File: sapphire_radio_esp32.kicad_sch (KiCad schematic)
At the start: 105 parts, among them IC1 AZ1117CH-3.3TRG1, J1 USB4105-GF-A, J2 Screw_Terminal_01x02, J3 FAKRA, J4 Screw_Terminal_01x02, J5 Screw_Terminal_01x02, Q1 DMG2305UX-7, Q3 2N7002PS_115, U1 ESP32-WROOM-32E-N8R2, U2 CP2102N-A02-GQFN24R, U4 SI4735, U5 NC7WZ14P6X, U6 TMUX1574PWR, U7 PCM5122PWR, U8 MAX9744ETH_

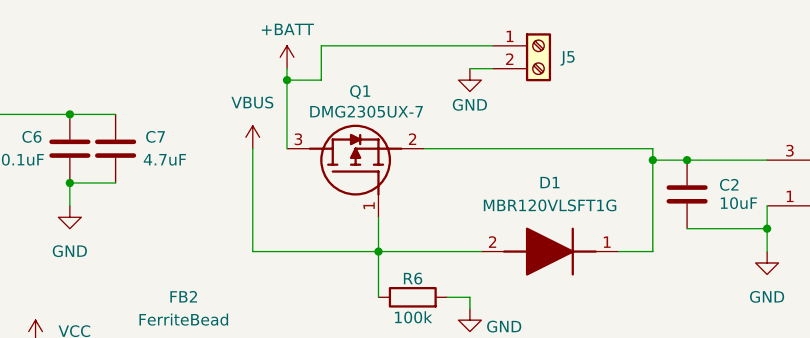
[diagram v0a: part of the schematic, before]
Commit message: Add fuse holder
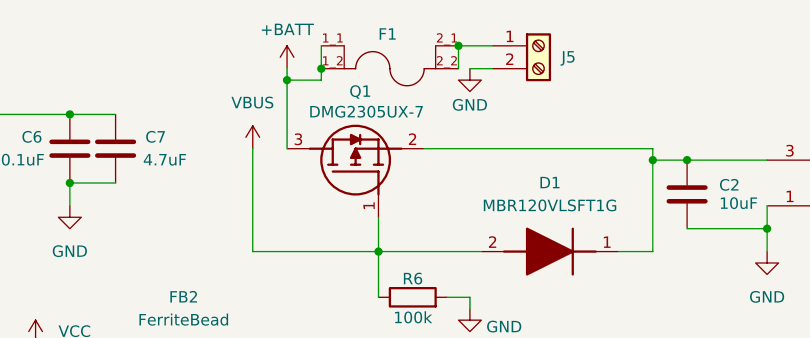
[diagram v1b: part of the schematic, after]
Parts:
- added F1: 3549-2, carter_kicad_footprints:FUSE_3549-2, symbol carter_kicad_symbols:3549-2 Mini Fuse Holder
- C10, C39: DigikeyPN (none) -> 732-8511-1-ND; MFN (none) -> Würth Elektronik; MPN (none) -> 865080545012
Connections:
- net +BATT: now also F1.1_1, F1.1_2; no longer J5.1 (Pin_1)
- new net: F1.2_1, F1.2_2, J5.1 (Pin_1)
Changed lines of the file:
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@@
 	(title_block
 		(title "Volkswagen Sapphire Radio Conversion")
-		(date "2026-03-21")
+		(date "2026-03-27")
 		(rev "1")
 		(company "Carter Harris - KE8OHO")
@@
 	)
 	(junction
+		(at 184.15 17.78)
+		(diameter 0)
+		(color 0 0 0 0)
+	)
+	(junction
 		(at 294.64 154.94)
 		(diameter 0)
@@
 	)
 	(junction
+		(at 199.39 15.24)
+		(diameter 0)
+		(color 0 0 0 0)
+	)
+	(junction
 		(at 153.67 113.03)
 		(diameter 0)
@@
 	(wire
 		(pts
+			(xy 184.15 15.24) (xy 184.15 17.78)
+		)
+		(stroke
+			(width 0)
+			(type default)
+		)
+	)
+	(wire
+		(pts
 			(xy 100.33 168.91) (xy 107.95 168.91)
 		)
@@
 	(wire
 		(pts
+			(xy 199.39 15.24) (xy 199.39 17.78)
+		)
+		(stroke
+			(width 0)
+			(type default)
+		)
+	)
+	(wire
+		(pts
 			(xy 226.06 142.24) (xy 232.41 142.24)
 		)
@@
 	(wire
 		(pts
+			(xy 199.39 15.24) (xy 203.2 15.24)
+		)
+		(stroke
+			(width 0)
+			(type default)
+		)
+	)
+	(wire
+		(pts
 			(xy 302.26 57.15) (xy 302.26 54.61)
 		)
@@
 	(wire
 		(pts
-			(xy 203.2 15.24) (xy 184.15 15.24)
-		)
-		(stroke
-			(width 0)
-			(type default)
-		)
-	)
-	(wire
-		(pts
 			(xy 294.64 71.12) (xy 294.64 67.31)
 		)
@@
 	(wire
 		(pts
-			(xy 184.15 15.24) (xy 184.15 19.05)
-		)
-		(stroke
-			(width 0)
-			(type default)
-		)
-	)
-	(wire
-		(pts
 			(xy 153.67 100.33) (xy 153.67 102.87)
 		)
@@
 	(wire
 		(pts
+			(xy 184.15 17.78) (xy 184.15 19.05)
+		)
+		(stroke
+			(width 0)
+			(type default)
+		)
+	)
+	(wire
+		(pts
 			(xy 334.01 97.79) (xy 337.82 97.79)
 		)
@@
 	)
 	(symbol
+		(lib_id "carter_kicad_symbols:3549-2 Mini Fuse Holder")
+		(at 191.77 17.78 0)
+		(unit 1)
+		(exclude_from_sim no)
+		(in_bom yes)
+		(on_board yes)
+		(dnp no)
+		(property "Reference" "F1"
+			(at 191.516 13.97 0)
+			(effects
+				(font
+					(size 1.27 1.27)
+				)
+			)
+		)
+		(property "Value" "3549-2"
+			(at 189.23 22.86 0)
+			(effects
+				(font
+					(size 1.27 1.27)
+				)
+				(justify left bottom)
+				(hide yes)
+			)
+		)
+		(property "Footprint" "carter_kicad_footprints:FUSE_3549-2"
+			(at 192.024 5.842 0)
+			(effects
+				(font
+					(size 1.27 1.27)
+				)
+				(justify bottom)
+				(hide yes)
+			)
+		)
+		(property "Datasheet" "https://www.keyelco.com/userAssets/file/K75p48.pdf"
+			(at 191.77 17.78 0)
+			(effects
+				(font
+					(size 1.27 1.27)
+				)
+				(hide yes)
+			)
+		)
+		(property "Description" "Fuse Block 20 A 500V 1 Circuit Blade Through Hole"
+			(at 191.77 17.78 0)
+			(effects
+				(font
+					(size 1.27 1.27)
+				)
+				(hide yes)
+			)
+		)
+		(property "MFN" "Keystone Electronics"
+			(at 192.024 5.842 0)
+			(effects
+				(font
+					(size 1.27 1.27)
+				)
+				(justify bottom)
+				(hide yes)
+			)
+		)
+		(property "MPN" "3549-2"
+			(at 191.77 17.78 0)
+			(effects
+				(font
+					(size 1.27 1.27)
+				)
+				(hide yes)
+			)
+		)
+		(property "DigikeyPN" "36-3549-2-ND"
+			(at 191.77 17.78 0)
+			(effects
+				(font
+					(size 1.27 1.27)
+				)
+				(hide yes)
+			)
+		)
+		(property "LCSCPN" "C3206081"
+			(at 191.77 17.78 0)
+			(effects
+				(font
+					(size 1.27 1.27)
+				)
+				(hide yes)
+			)
+		)
+		(pin "2_2"
+		)
+		(pin "2_1"
+		)
+		(pin "1_2"
+		)
+		(pin "1_1"
+		)
+		(instances
+			(project ""
+				(path "/b2cc6a8e-d718-44b3-b274-265d252d3f92"
+					(reference "F1")
+					(unit 1)
+				)
+			)
+		)
+	)
+	(symbol
 		(lib_id "Device:C")
 		(at 330.2 115.57 90)
@@
 			)
 		)
+		(property "MFN" "Würth Elektronik"
+			(at 317.5 58.42 0)
+			(effects
+				(font
+					(size 1.27 1.27)
+				)
+				(hide yes)
+			)
+		)
+		(property "MPN" "865080545012"
+			(at 317.5 58.42 0)
+			(effects
+				(font
+					(size 1.27 1.27)
+				)
+				(hide yes)
+			)
+		)
+		(property "DigikeyPN" "732-8511-1-ND"
+			(at 317.5 58.42 0)
+			(effects
+				(font
+					(size 1.27 1.27)
+				)
+				(hide yes)
+			)
+		)
 		(pin "2"
 		)
@@
 			(at 314.96 71.12 0)
 			(effects
+				(font
+					(size 1.27 1.27)
+				)
+				(hide yes)
+			)
+		)
+		(property "MFN" "Würth Elektronik"
+			(at 314.96 71.12 0)
+			(effects
+				(font
+					(size 1.27 1.27)
+				)
+				(hide yes)
+			)
+		)
+		(property "MPN" "865080545012"
+			(at 314.96 71.12 0)
+			(effects
+				(font
+					(size 1.27 1.27)
+				)
+				(hide yes)
+			)
+		)
+		(property "DigikeyPN" "732-8511-1-ND"
+			(at 314.96 71.12 0)
+			(effects

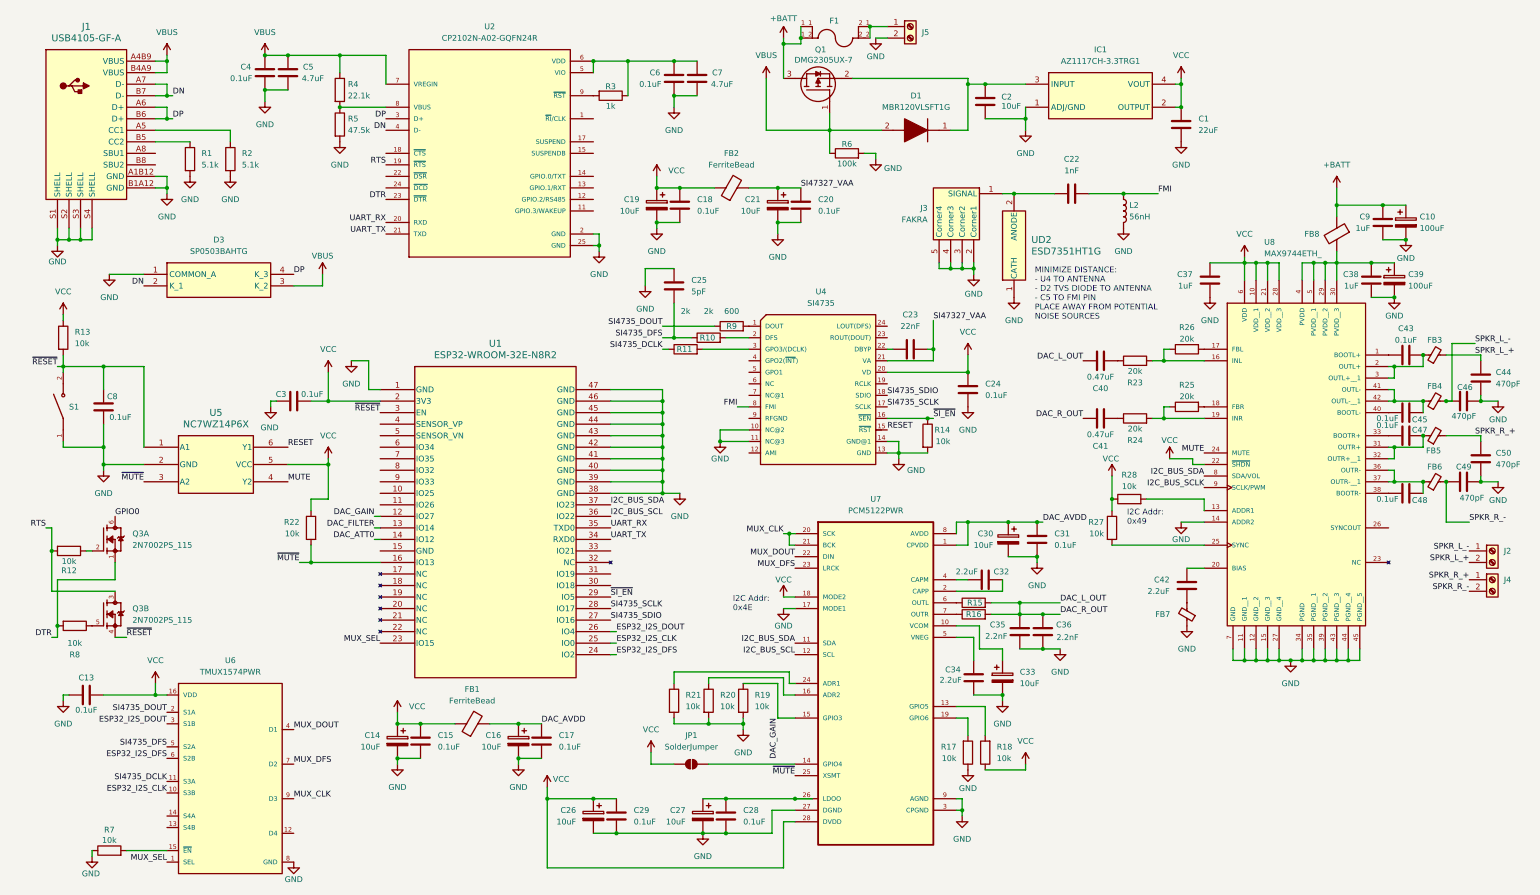
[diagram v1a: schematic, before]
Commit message: Add power filtering and pots
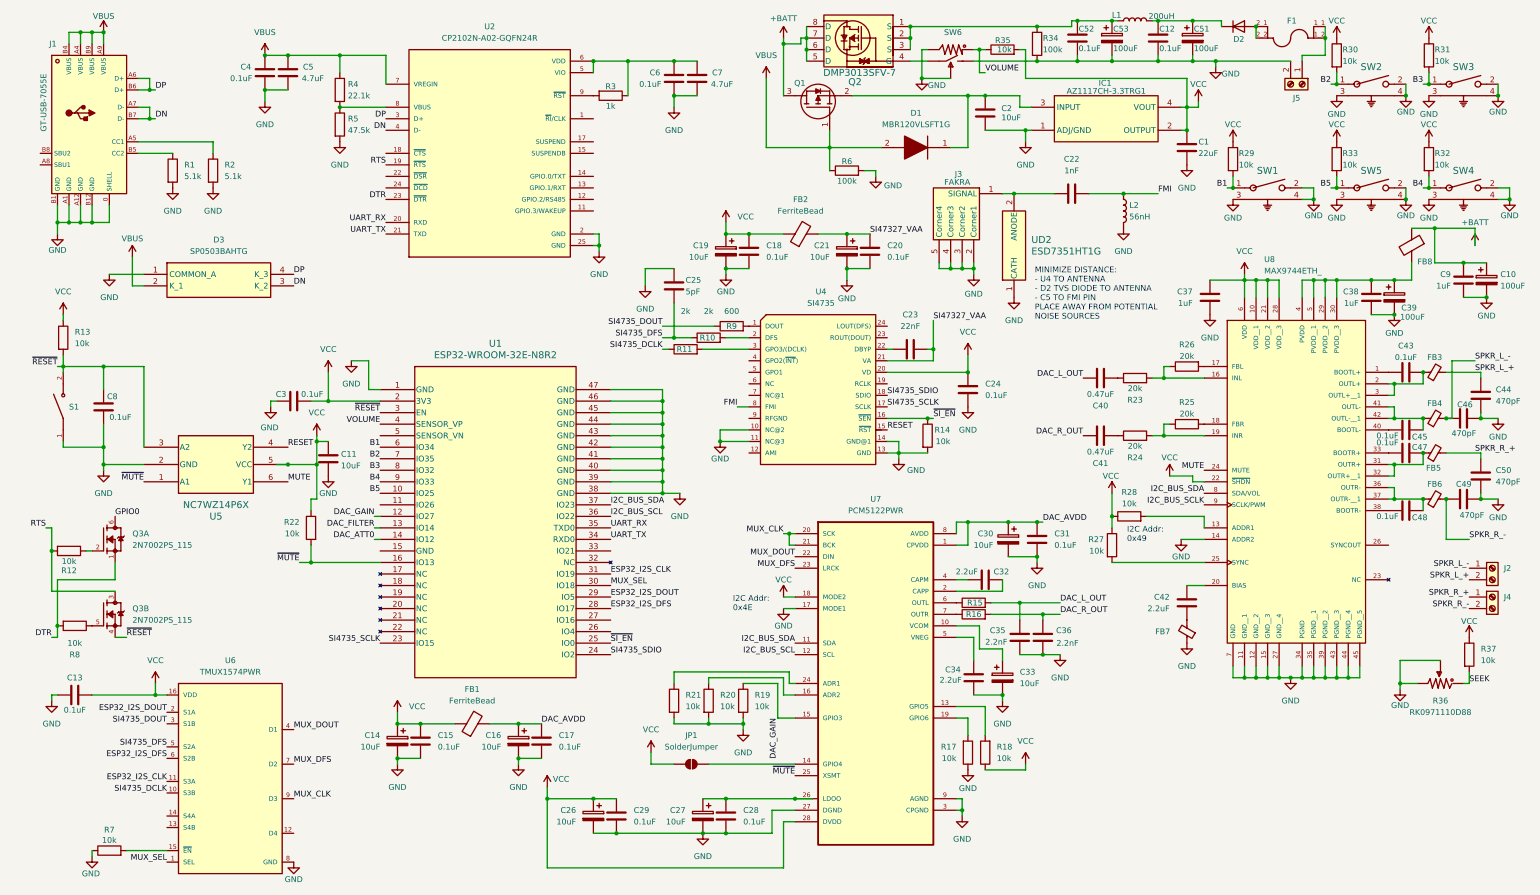
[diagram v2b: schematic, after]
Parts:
- removed J1: USB4105-GF-A, carter_kicad_footprints:USB4105-GF-A_1, symbol carter_kicad_symbols:USB4105-GF-A USB-C Socket
- added C11: 10uF, Capacitor_SMD:C_0603_1608Metric, symbol Device:C
- added C12, C52: 0.1uF, Capacitor_SMD:C_0603_1608Metric, symbol Device:C
- added C51, C53: 100uF, carter_kicad_footprints:CAP_6.3_6.3, symbol Device:C_Polarized
- added D2: D, Package_TO_SOT_SMD:TO-252-2, symbol Device:D
- added J1: GT-USB-7055E, carter_kicad_footprints:USB-C-SMD_GT-USB-7055E, symbol carter_kicad_symbols:GT-USB-7055E USB-C Vertical Socket (LCSC Only)
- added L1: 200uH, carter_kicad_footprints:IND-SMD_L28.0-W25.0-74437529203331, symbol Device:L
- added Q2: DMP3013SFV-7, carter_kicad_footprints:POWERDI3333-8_UX_DIO, symbol carter_kicad_symbols:DMP3013SFV-7 10A P-Channel MOSFET
- added R29, R30, R31, R32, R33, R35, R37: 10k, Resistor_SMD:R_0603_1608Metric, symbol Device:R
- added R34: 100k, Resistor_SMD:R_0603_1608Metric, symbol Device:R
- added R36: RK0971110D88, carter_kicad_footprints:RES-ADJ-TH_RK097111080R, symbol carter_kicad_symbols:RK0971110D88 10k Potentiometer
- added SW1, SW2, SW3, SW4, SW5: 1825027-8, carter_kicad_footprints:SW2_1825027-C_TEC, symbol carter_kicad_symbols:1825027-8 Right Angle Button
- added SW6: RK09711110EL, carter_kicad_footprints:RES-ADJ-TH_RK09711110EL, symbol carter_kicad_symbols:RK09711110EL Potentiometer w/ Rotary Button
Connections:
- net +BATT: now also Q2.5 (D), Q2.6 (D), Q2.7 (D), Q2.8 (D); no longer F1.1_1, F1.1_2
- net DAC_L_OUT: no longer C36.1, C41.1, R16.2
- net DN: now also D3.3 (K_2), J1.A7 (D-), J1.B7 (D-); no longer D3.2 (K_1)
- net DP: now also J1.A6 (D+), J1.B6 (D+)
- net ESP32_I2S_CLK: now also U1.31 (IO19), U6.11 (S3A); no longer U1.25 (IO0), U6.10 (S3B)
- net ESP32_I2S_DFS: now also U1.28 (IO17); no longer U1.24 (IO2)
- net ESP32_I2S_DOUT: now also U1.29 (IO5), U6.2 (S1A); no longer U1.26 (IO4), U6.3 (S1B)
- net GND: now also C11.2, C12.2, C51.2, C52.2, C53.2, J1.0 (SHELL), J1.A1 (GND), J1.A12 (GND), J1.B1 (GND), J1.B12 (GND), R34.2, R36.2, R36.3, SW1.2, SW1.3, SW1.4, SW2.2, SW2.3, SW2.4, SW3.2, SW3.3, SW3.4, SW4.2, SW4.3, SW4.4, SW5.2, SW5.3, SW5.4, SW6.2, SW6.3, SW6.5
- net MUTE: now also U5.6 (Y1); no longer U5.4 (Y2)
- net MUX_SEL: now also U1.30 (IO18); no longer U1.23 (IO15)
- net RESET: now also U5.4 (Y2); no longer U5.6 (Y1)
- net SI4735_DCLK: now also U6.10 (S3B); no longer U6.11 (S3A)
- net SI4735_DOUT: now also U6.3 (S1B); no longer U6.2 (S1A)
- net SI4735_SCLK: now also U1.23 (IO15); no longer U1.28 (IO17)
- net SI4735_SDIO: now also U1.24 (IO2); no longer U1.27 (IO16)
- net VBUS: now also D3.2 (K_1), J1.A4 (VBUS), J1.A9 (VBUS), J1.B4 (VBUS), J1.B9 (VBUS); no longer D3.3 (K_2)
- net VCC: now also C11.1, R29.1, R30.1, R31.1, R32.1, R33.1, R35.2, R37.1
- net ~{MUTE}: now also U5.1 (A1); no longer U5.3 (A2)
- net ~{RESET}: now also U5.3 (A2); no longer U5.1 (A1)
- net ~{SI_EN}: now also U1.25 (IO0); no longer U1.29 (IO5)
- net at R2.1: now also J1.A5 (CC1)
- net at R1.1: now also J1.B5 (CC2)
- net at F1.2_1, F1.2_2: now also D2.2 (A); no longer J5.1 (Pin_1)
- net B5: now reaches U1.10 (IO25)
- net B5: now also R33.2, SW5.1
- net VOLUME: now reaches U1.4 (SENSOR_VP)
- net VOLUME: now also R35.1, SW6.4
- net B1: now reaches U1.6 (IO34)
- net B1: now also R29.2, SW1.1
- net B2: now reaches U1.7 (IO35)
- net B2: now also R30.2, SW2.1
- net B3: now reaches U1.8 (IO32)
- net B3: now also R31.2, SW3.1
- net B4: now reaches U1.9 (IO33)
- net B4: now also R32.2, SW4.1
- new net: C12.1, C51.1, D2.1 (K), L1.2
- new net: F1.1_1, F1.1_2, J5.1 (Pin_1)
- new net: C52.1, C53.1, L1.1, Q2.1 (S), Q2.2 (S), Q2.3 (S), R34.1
- new net: Q2.4 (G), SW6.1
- new net DAC_R_OUT: C36.1, C41.1, R16.2
- new net SEEK: R36.1, R37.2
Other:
- moved on the sheet: C1, C10, C13, C18, C19, C2, C20, C21, C35, C36, C37, C38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

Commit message: Add board first pass; move ESP32 GPIO to allow easier routing
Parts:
- removed C30: 10uF, Capacitor_SMD:CP_Elec_4x5.4, symbol Device:C_Polarized
- added D4: LED, Connector_JST:JST_ZH_B2B-ZR-SM4-TF_1x02-1MP_P1.50mm_Vertical, symbol Device:LED
- added J6: Conn_01x03, Connector_JST:JST_PH_B3B-PH-SM4-TB_1x03-1MP_P2.00mm_Vertical, symbol Connector_Generic:Conn_01x03
- added R38: 5, Resistor_SMD:R_0603_1608Metric, symbol Device:R
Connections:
- net I2C_BUS_SCLK is gone; now on net I2C_BUS_SCL: U8.9 (SCLK/PWM)
- net B1: now also U1.27 (IO16); no longer U1.6 (IO34)
- net B2: now also U1.28 (IO17); no longer U1.7 (IO35)
- net B3: now also U1.29 (IO5); no longer U1.8 (IO32)
- net B4: now also U1.30 (IO18); no longer U1.9 (IO33)
- net B5: now also U1.31 (IO19); no longer U1.10 (IO25)
- net DAC_FILTER: now also U1.25 (IO0); no longer U1.13 (IO14)
- net DAC_GAIN: now also U1.23 (IO15); no longer U1.12 (IO27)
- net ESP32_I2S_CLK: now also U1.10 (IO25); no longer U1.31 (IO19)
- net ESP32_I2S_DFS: now also U1.8 (IO32); no longer U1.28 (IO17)
- net ESP32_I2S_DOUT: now also U1.16 (IO13); no longer U1.29 (IO5)
- net GND: now also U1.15 (GND), J6.3 (Pin_3), R38.2
- net I2C_BUS_SDA: now also U1.33 (IO21); no longer U1.37 (IO23)
- net MUX_SEL: now also U1.24 (IO2); no longer U1.30 (IO18)
- net SEEK: now also U1.5 (SENSOR_VN)
- net SI4735_SCLK: now also U1.12 (IO27); no longer U1.23 (IO15)
- net SI4735_SDIO: now also U1.11 (IO26); no longer U1.24 (IO2)
- net VCC: now also U1.9 (IO33), D4.2 (A), J6.2 (Pin_2)
- net ~{MUTE}: no longer R22.2, U1.16 (IO13), U5.1 (A1)
- net ~{SI_EN}: now also U1.13 (IO14); no longer U1.25 (IO0)
- net DIAL_SERVO: now reaches U1.26 (IO4)
- net DIAL_SERVO: now also J6.1 (Pin_1)
- new net: R22.2, U5.1 (A1)
- new net: D4.1 (K), R38.1
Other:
- moved on the sheet: C11, R22, U1

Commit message: Final WROOM revision
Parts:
- removed U2: CP2102N-A02-GQFN24R, carter_kicad_footprints:QFN50P400X400X80-25N, symbol carter_kicad_symbols:CP2102N USB-UART Bridge
- added C30: 0.47uF, Capacitor_SMD:C_0603_1608Metric, symbol Device:C
- added IC2: AS169-73LF, carter_kicad_footprints:SOT95P270X145-6N, symbol carter_kicad_symbols:AS169-73LF
- added IC3: CP2102N-A02-GQFN28R, carter_kicad_footprints:QFN50P700X700X80-45N, symbol carter_kicad_symbols:CP2102N-A02-GQFN28R USB-UART Bridge
- added R39, R40, R41: 10k, Resistor_SMD:R_0603_1608Metric, symbol Device:R
- added U3: NC7WZ14P6X, carter_kicad_footprints:SC70-6_ONS, symbol carter_kicad_symbols:NC7WZ14P6X Dual Channel Inverter
- C40, C41: DigikeyPN (none) -> 490-3291-1-ND; LCSCPN (none) -> C77052; MFN (none) -> Murata Electronics; MPN (none) -> GRM188R71E474KA12D
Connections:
- net DN: now also IC3.5 (D-)
- net DP: now also IC3.4 (D+)
- net DTR: now also IC3.28 (DTR)
- net FMI: now also C22.1, IC2.1 (J3); no longer C22.2, L2.1, U4.8 (FMI)
- net GND: now also U4.9 (RFGND), IC2.2 (GND), IC3.29 (GND_2), IC3.3 (GND_1), R39.2, R40.2, R41.1, U3.2 (GND)
- net RTS: now also IC3.24 (RTS)
- net UART_RX: now also IC3.25 (RXD)
- net UART_TX: now also IC3.26 (TXD)
- net VBUS: now also IC3.7 (VREGIN)
- net VCC: now also U3.5 (VCC)
- net at C6.1, C7.1, R3.1: now also IC3.6 (VDD)
- net at R3.2: now also IC3.9 (RSTB)
- net at U4.12 (AMI): now also C30.2
- net at R4.2, R5.1: now also IC3.8 (VBUS)
- net at J3.1 (SIGNAL), UD2.2 (ANODE): now also IC2.5 (J1); no longer C22.1
- net FM_SEL: now reaches U1.37 (IO23)
- net FM_SEL: now also IC2.6 (V2), R40.1, R41.2, U3.1 (A1)
- new net: C22.2, L2.1, U4.8 (FMI)
- new net AM: C30.1, IC2.3 (J2)
- new net AM_SEL: IC2.4 (V1), R39.1, U3.6 (Y1)
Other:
- moved on the sheet: C22, C4, C5, C6, C7, D3, J6, L2, R3, R4, R5, UD2
